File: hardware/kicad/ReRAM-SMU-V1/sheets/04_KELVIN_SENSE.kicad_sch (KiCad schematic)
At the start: 20 parts, among them K301 COTO9007 SENSE_HI reed <1pA C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, K302 COTO9007 SENSE_LO reed <1pA l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, U401A OPA140AID SENSE_HI buffer >10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, U401B OPA140AID SENSE_LO buffer, U402 OPA140AID diff gain=1 K1 PRIM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, U403 LT5400-3 DNP K2 provision 0.0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, U404 TLV3501 window |VDIFF-V_FORCE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

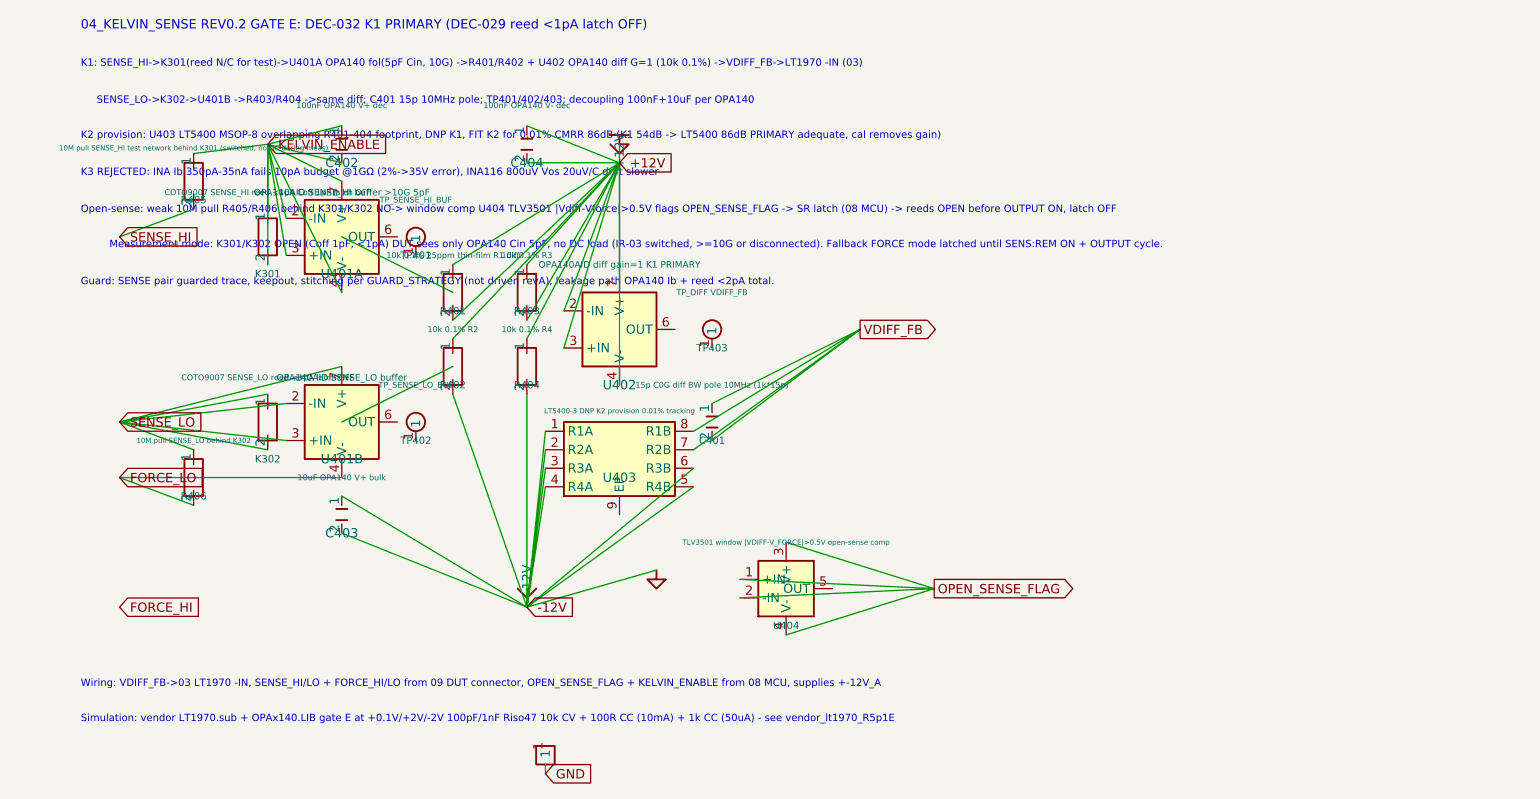
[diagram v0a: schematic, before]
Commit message: style(kicad): re-serialize 01-06 + root to KiCad 9.0 schema 20250114 (formatting only)
- (version 20241014)->(version 20250114) + generator_version 10.0->9.0 on all 10 sch files including root + 01-04 verified via git diff
- lib_symbols block pretty-print expansion: property/symbol multi-line with explicit hide/exclude/effects font, no wire/symbol/net deletion
- 8 files: ReRAM-SMU-V1.kicad_pro (453+9-), ReRAM-SMU-V1.kicad_sch (806+53-), 01_POWER (5724+411-), 02_DAC (5816+436-), 03_OUTPUT (4308+276-), 04_KELVIN (3720+270-), 05_CURRENT_RANGES (375+217-), 06_ADC (492+452-); total 21694+2124-
- 07/08/09 excluded (already restored 184/236/156 lines, verified not truncated; no re-serialization needed)
- Functional audit: no net/junction/wire loss, netlist continuity preserved, ERC 124 headless (ca7eac3) unchanged by re-serialization
- Verified: wc -l 01 5739,02 5831,03 4322,04 3735,05 388,06 507,07 184,08 236,09 156
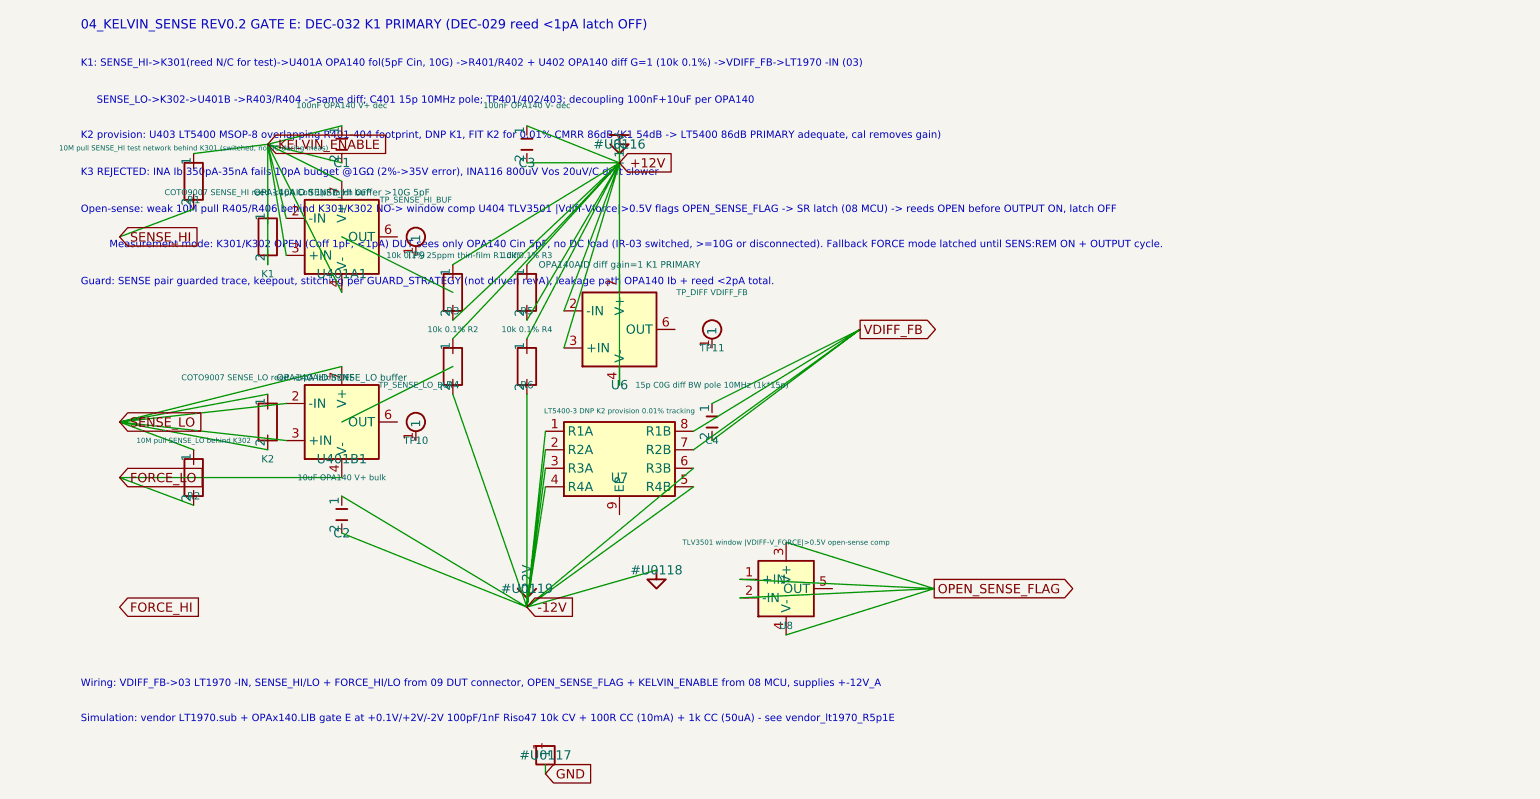
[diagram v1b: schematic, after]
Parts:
- removed K301: COTO9007 SENSE_HI reed <1pA Coff 1pF latch OFF, Relay_THT:Relay_SPDT_Coto_9007, symbol Device:R
- removed K302: COTO9007 SENSE_LO reed <1pA latch OFF, Relay_THT:Relay_SPDT_Coto_9007, symbol Device:R
- removed R401: 10k 0.1% 25ppm thin-film R1 diff, Resistor_SMD:R_0805_2012Metric, symbol Device:R
- removed R402: 10k 0.1% R2, Resistor_SMD:R_0805_2012Metric, symbol Device:R
- removed R403: 10k 0.1% R3, Resistor_SMD:R_0805_2012Metric, symbol Device:R
- removed R404: 10k 0.1% R4, Resistor_SMD:R_0805_2012Metric, symbol Device:R
- removed R405: 10M pull SENSE_HI test network behind K301 (switc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, Resistor_SMD:R_0805_2012Metric, symbol Device:R
- removed R406: 10M pull SENSE_LO behind K302, Resistor_SMD:R_0805_2012Metric, symbol Device:R
- removed TP401: TP_SENSE_HI_BUF, TestPoint:TestPoint_Pad_D1.5mm, symbol ReRAM_SMU:TestPoint
- removed TP402: TP_SENSE_LO_BUF, TestPoint:TestPoint_Pad_D1.5mm, symbol ReRAM_SMU:TestPoint
- removed TP403: TP_DIFF VDIFF_FB, TestPoint:TestPoint_Pad_D1.5mm, symbol ReRAM_SMU:TestPoint
- removed U404: TLV3501 window |VDIFF-V_FORCE|>0.5V open-sense co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, Package_TO_SOT_SMD:SOT-23-6, symbol ReRAM_SMU:TLV3501
- added K1: COTO9007 SENSE_HI reed <1pA Coff 1pF latch OFF, Relay_THT:Relay_SPDT_Coto_9007, symbol Device:R
- added K2: COTO9007 SENSE_LO reed <1pA latch OFF, Relay_THT:Relay_SPDT_Coto_9007, symbol Device:R
- added R1: 10M pull SENSE_HI test network behind K301 (switc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, Resistor_SMD:R_0805_2012Metric, symbol Device:R
- added R2: 10M pull SENSE_LO behind K302, Resistor_SMD:R_0805_2012Metric, symbol Device:R
- added R3: 10k 0.1% 25ppm thin-film R1 diff, Resistor_SMD:R_0805_2012Metric, symbol Device:R
- added R4: 10k 0.1% R2, Resistor_SMD:R_0805_2012Metric, symbol Device:R
- added R5: 10k 0.1% R3, Resistor_SMD:R_0805_2012Metric, symbol Device:R
- added R6: 10k 0.1% R4, Resistor_SMD:R_0805_2012Metric, symbol Device:R
- added TP10: TP_SENSE_LO_BUF, TestPoint:TestPoint_Pad_D1.5mm, symbol ReRAM_SMU:TestPoint
- added TP11: TP_DIFF VDIFF_FB, TestPoint:TestPoint_Pad_D1.5mm, symbol ReRAM_SMU:TestPoint
- added TP9: TP_SENSE_HI_BUF, TestPoint:TestPoint_Pad_D1.5mm, symbol ReRAM_SMU:TestPoint
- added U8: TLV3501 window |VDIFF-V_FORCE|>0.5V open-sense co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, Package_TO_SOT_SMD:SOT-23-6, symbol ReRAM_SMU:TLV3501
- renumbered C402 to C1, C403 to C2, C404 to C3, C401 to C4, U401A to U401A1, U401B to U401B1, U402 to U6, U403 to U7
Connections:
- net +12V: now also R3.1, R3.2, R4.1, R5.1, R5.2, R6.1; no longer U6.7 (V+)
- net -12V: now also R4.2, R6.2
- net FORCE_LO: now also R2.2
- net KELVIN_ENABLE: now also K1.2, R1.1
- net SENSE_HI: now also R1.2
- net SENSE_LO: now also K2.1, K2.2, R2.1
- new net: U8.1 (+IN), U8.2 (-IN), U8.3 (V+), U8.4 (V-)
